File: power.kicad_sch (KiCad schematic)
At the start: 6 parts, among them J5 power, U7 Buck

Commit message: redone the switch connectors to accomodate a current sense print. Rearranged parts and updated silk texts to be 50% of their original size
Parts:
- renumbered C6 to C501, C7 to C502, D6 to D501, D7 to D502, J5 to J501, U7 to U501
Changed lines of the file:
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@@
   (symbol (lib_id "Device:D") (at 128.27 69.85 0) (mirror y) (unit 1)
     (in_bom yes) (on_board yes) (fields_autoplaced)
-    (property "Reference" "D6" (id 0) (at 128.27 64.8802 0))
+    (property "Reference" "D501" (id 0) (at 128.27 64.8802 0))
     (property "Value" "D" (id 1) (at 128.27 67.4171 0))
     (property "Footprint" "Diode_THT:D_DO-34_SOD68_P7.62mm_Horizontal" (id 2) (at 128.27 69.85 0)
@@
   (symbol (lib_id "power:GND") (at 175.26 83.82 0) (unit 1)
     (in_bom yes) (on_board yes) (fields_autoplaced)
-    (property "Reference" "#PWR0109" (id 0) (at 175.26 90.17 0)
+    (property "Reference" "#PWR0506" (id 0) (at 175.26 90.17 0)
       (effects (font (size 1.27 1.27)) hide)
     )
@@
   (symbol (lib_id "power:GND") (at 137.16 83.82 0) (unit 1)
     (in_bom yes) (on_board yes) (fields_autoplaced)
-    (property "Reference" "#PWR0122" (id 0) (at 137.16 90.17 0)
+    (property "Reference" "#PWR0502" (id 0) (at 137.16 90.17 0)
       (effects (font (size 1.27 1.27)) hide)
     )
@@
   (symbol (lib_id "power:GND") (at 127 83.82 0) (unit 1)
     (in_bom yes) (on_board yes) (fields_autoplaced)
-    (property "Reference" "#PWR0107" (id 0) (at 127 90.17 0)
+    (property "Reference" "#PWR0501" (id 0) (at 127 90.17 0)
       (effects (font (size 1.27 1.27)) hide)
     )
@@
   (symbol (lib_id "power:GND") (at 152.4 83.82 0) (unit 1)
     (in_bom yes) (on_board yes) (fields_autoplaced)
-    (property "Reference" "#PWR0123" (id 0) (at 152.4 90.17 0)
+    (property "Reference" "#PWR0503" (id 0) (at 152.4 90.17 0)
       (effects (font (size 1.27 1.27)) hide)
     )
@@
   (symbol (lib_id "power:+5V") (at 180.34 69.85 0) (unit 1)
     (in_bom yes) (on_board yes)
-    (property "Reference" "#PWR0116" (id 0) (at 180.34 73.66 0)
+    (property "Reference" "#PWR0507" (id 0) (at 180.34 73.66 0)
       (effects (font (size 1.27 1.27)) hide)
     )
@@
   (symbol (lib_id "custom_kicad_lib_sk:Buck") (at 144.78 72.39 0) (mirror y) (unit 1)
     (in_bom yes) (on_board yes) (fields_autoplaced)
-    (property "Reference" "U7" (id 0) (at 144.78 64.931 0))
+    (property "Reference" "U501" (id 0) (at 144.78 64.931 0))
     (property "Value" "Buck" (id 1) (at 144.78 67.4679 0))
     (property "Footprint" "custom_kicad_lib_sk:Buck" (id 2) (at 142.24 72.39 0)
@@
   (symbol (lib_id "Connector:Screw_Terminal_01x02") (at 118.11 69.85 0) (mirror y) (unit 1)
     (in_bom yes) (on_board yes) (fields_autoplaced)
-    (property "Reference" "J5" (id 0) (at 116.078 70.2853 0)
+    (property "Reference" "J501" (id 0) (at 116.078 70.2853 0)
       (effects (font (size 1.27 1.27)) (justify left))
     )
@@
   (symbol (lib_id "Device:C_Polarized") (at 175.26 77.47 0) (unit 1)
     (in_bom yes) (on_board yes) (fields_autoplaced)
-    (property "Reference" "C7" (id 0) (at 178.181 75.7463 0)
+    (property "Reference" "C502" (id 0) (at 178.181 75.7463 0)
       (effects (font (size 1.27 1.27)) (justify left))
     )
@@
   (symbol (lib_id "power:+5VA") (at 165.1 66.04 0) (unit 1)
     (in_bom yes) (on_board yes) (fields_autoplaced)
-    (property "Reference" "#PWR0117" (id 0) (at 165.1 69.85 0)
+    (property "Reference" "#PWR0504" (id 0) (at 165.1 69.85 0)
       (effects (font (size 1.27 1.27)) hide)
     )
@@
   (symbol (lib_id "Device:D") (at 170.18 69.85 180) (unit 1)
     (in_bom yes) (on_board yes) (fields_autoplaced)
-    (property "Reference" "D7" (id 0) (at 170.18 64.8802 0))
+    (property "Reference" "D502" (id 0) (at 170.18 64.8802 0))
     (property "Value" "D" (id 1) (at 170.18 67.4171 0))
     (property "Footprint" "Diode_THT:D_DO-34_SOD68_P7.62mm_Horizontal" (id 2) (at 170.18 69.85 0)
@@
   (symbol (lib_id "power:GND") (at 165.1 83.82 0) (unit 1)
     (in_bom yes) (on_board yes) (fields_autoplaced)
-    (property "Reference" "#PWR0108" (id 0) (at 165.1 90.17 0)
+    (property "Reference" "#PWR0505" (id 0) (at 165.1 90.17 0)
       (effects (font (size 1.27 1.27)) hide)
     )
@@
   (symbol (lib_id "Device:C_Polarized") (at 165.1 77.47 0) (unit 1)
     (in_bom yes) (on_board yes) (fields_autoplaced)
-    (property "Reference" "C6" (id 0) (at 168.021 75.7463 0)
+    (property "Reference" "C501" (id 0) (at 168.021 75.7463 0)
       (effects (font (size 1.27 1.27)) (justify left))
     )

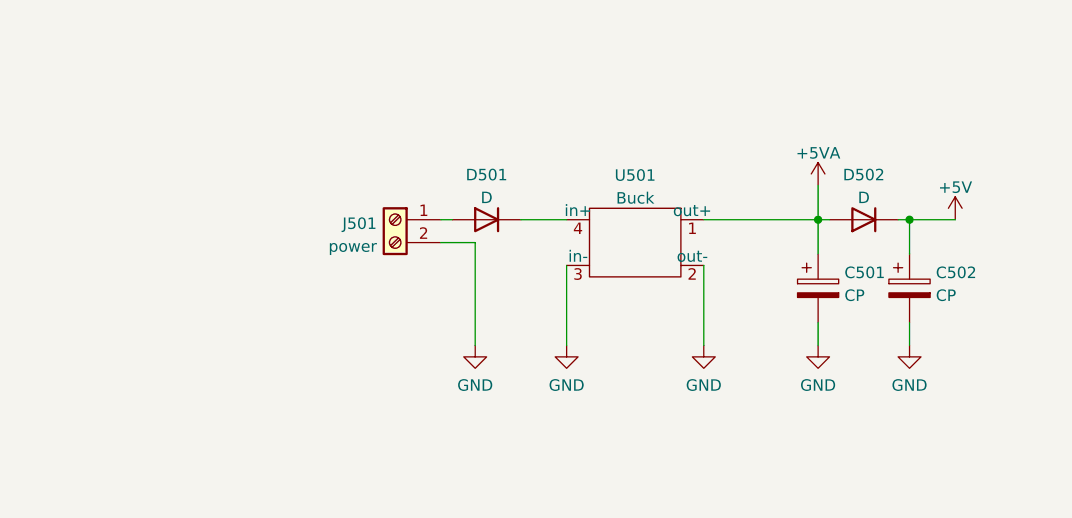
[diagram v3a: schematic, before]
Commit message: altered the code drastically and made a new PCB. PCB is still much work.
I finally fixed that issue where loco functions and speed were not serviced to the multimaus clients.
The Nx code also has been succesfully tested using the monitor.
MCP bug also has been solded. The bug was in assembleIO.py
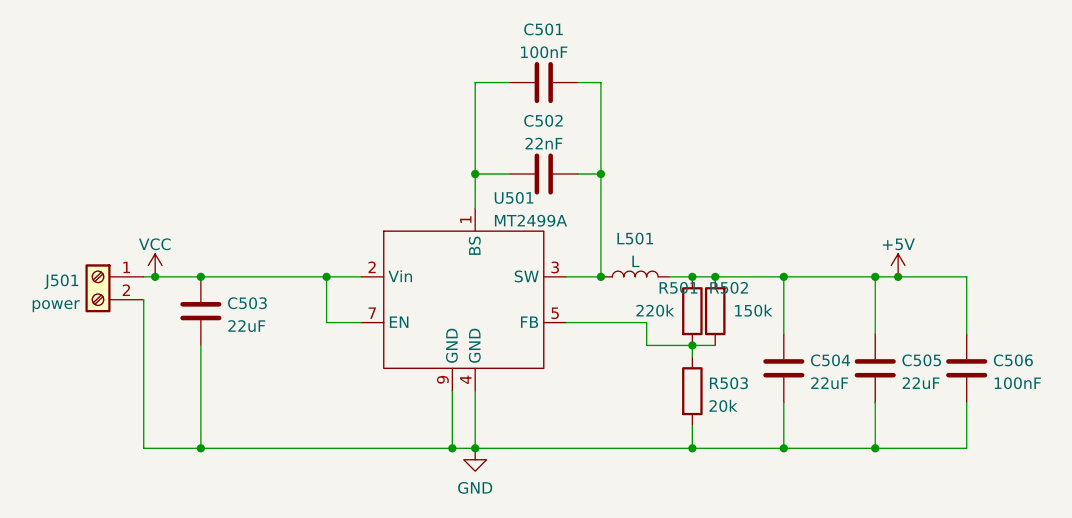
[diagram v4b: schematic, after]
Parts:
- removed C501, C502: CP, Capacitor_THT:CP_Radial_D8.0mm_P3.50mm, symbol Device:C_Polarized
- removed D501, D502: D, Diode_THT:D_DO-34_SOD68_P7.62mm_Horizontal, symbol Device:D
- removed U501: Buck, custom_kicad_lib_sk:Buck, symbol custom_kicad_lib_sk:Buck
- added C501, C506: 100nF, Capacitor_SMD:C_0402_1005Metric_Pad0.74x0.62mm_HandSolder, symbol Device:C
- added C502: 22nF, Capacitor_SMD:C_0402_1005Metric_Pad0.74x0.62mm_HandSolder, symbol Device:C
- added C503, C504, C505: 22uF, Capacitor_SMD:C_0603_1608Metric_Pad1.08x0.95mm_HandSolder, symbol Device:C
- added L501: L, Inductor_SMD:L_Bourns-SRU8028_8.0x8.0mm, symbol Device:L
- added R501: 220k, Resistor_SMD:R_0603_1608Metric_Pad0.98x0.95mm_HandSolder, symbol Device:R
- added R502: 150k, Resistor_SMD:R_0603_1608Metric_Pad0.98x0.95mm_HandSolder, symbol Device:R
- added R503: 20k, Resistor_SMD:R_0603_1608Metric_Pad0.98x0.95mm_HandSolder, symbol Device:R
- added U501: MT2499A, Package_SO:TI_SO-PowerPAD-8, symbol custom_kicad_lib_sk:MT499A
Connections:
- net +5V: now also C504.1, C505.1, C506.1, L501.2, R501.1, R502.2
- net GND: now also C503.2, C504.2, C505.2, C506.2, R503.2, U501.4 (GND), U501.9 (GND)
- net VCC: now reaches J501.1 (Pin_1)
- net VCC: now also C503.1, U501.2 (Vin), U501.7 (EN)
- new net: R501.2, R502.1, R503.1, U501.5 (FB)
- new net: C501.1, C502.1, U501.1 (BS)
- new net: C501.2, C502.2, L501.1, U501.3 (SW)
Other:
- moved on the sheet: J501
